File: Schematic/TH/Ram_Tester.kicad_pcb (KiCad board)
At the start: 2 copper layers, 63.3 x 57.2 mm, 42 parts, among them J1 Conn_01x02_Pin, J2 ICSP, Q1 2N7000, Q2 2N7000, SW1 SW_DIP_x03, SW2 SW_Push, U1 ATmega328-P, U2 RAM / ZIF, U3 ZIP Socket, Y1 Crystal

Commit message: v1.1 - minor fix
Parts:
- C5: footprint Capacitor_THT:C_Disc_D4.3mm_W1.9mm_P5.00mm -> Capacitor_THT:CP_Radial_D4.0mm_P2.00mm
- moved C5 2.00 mm to (117.6, 77.0)
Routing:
- net /5V: track 124.3 -> 130.3 mm
- net /GND: track 198.9 -> 199.9 mm, vias 40 -> 38
- net Net-(U1-PC3): track 18.2 -> 18.8 mm

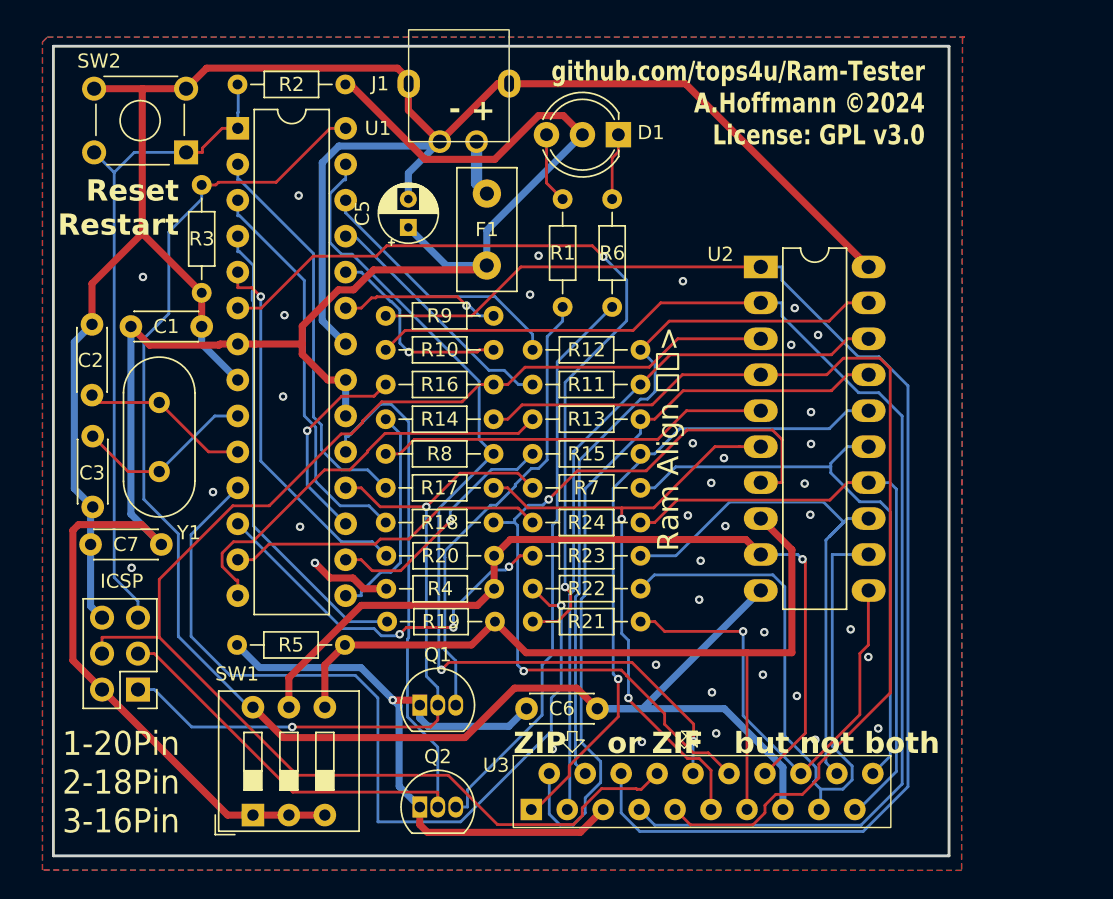
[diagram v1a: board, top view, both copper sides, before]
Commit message: v2 TH Version with Display
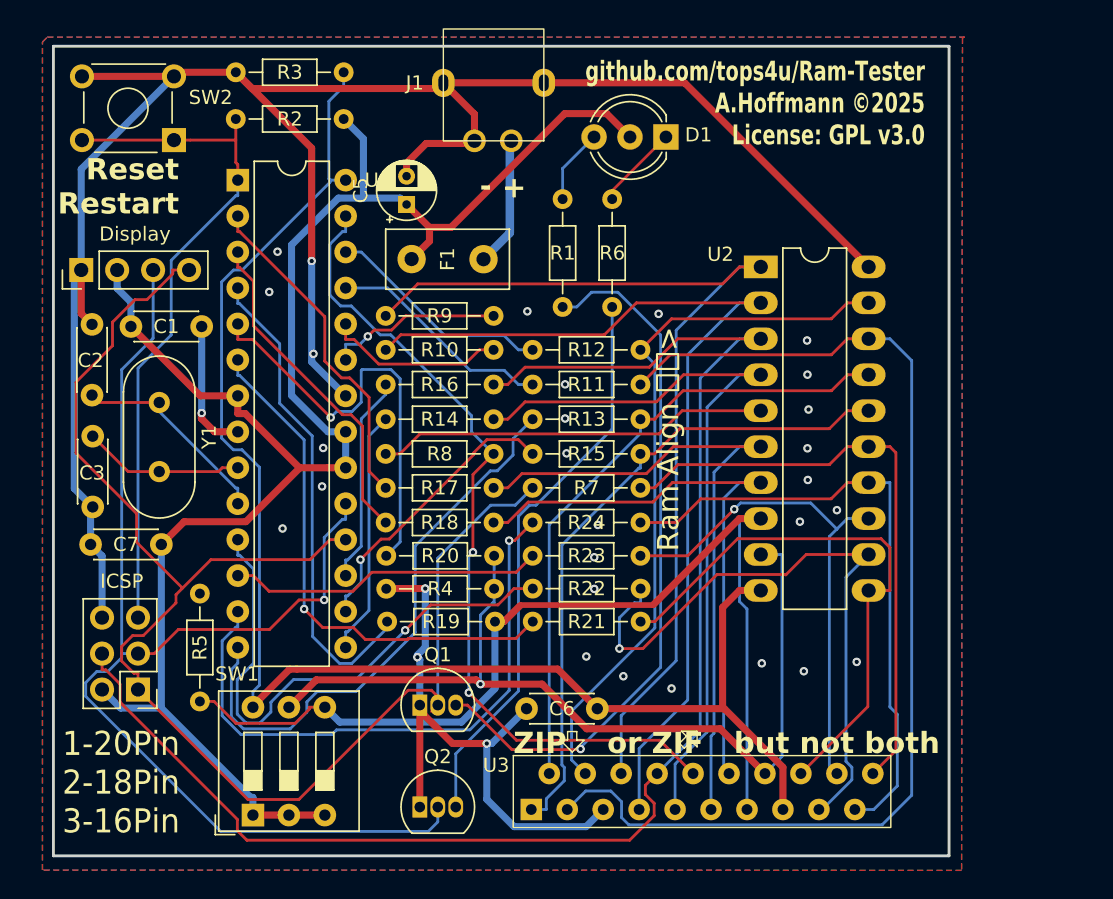
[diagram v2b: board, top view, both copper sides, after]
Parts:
- added Display: Conn_01x04_Pin, Connector_PinHeader_2.54mm:PinHeader_1x04_P2.54mm_Vertical, F.Cu at (94.5, 80.0)
- Y1: footprint Crystal:Crystal_HC49-U_Vertical -> Crystal:Crystal_HC49-4H_Vertical
- moved R3 15.8 mm to (105.4, 66.0), turned to 0 degrees
- moved F1 4.64 mm to (122.9, 79.2), turned to 180 degrees
- moved R5 4.48 mm to (102.9, 102.9), turned to -90 degrees
- moved U1 3.66 mm to (105.5, 73.7)
- moved D1 3.36 mm to (135.8, 70.6)
- moved J1 2.45 mm to (123.6, 76.9)
- moved R2 2.44 mm to (113.0, 69.3)
- moved C5 1.62 mm to (117.5, 75.4)
- moved SW2 1.22 mm to (101.0, 70.8)
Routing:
- net Net-(Display1-Pin_4): track 53.1 -> 101.2 mm, vias 2 -> 0
- net Net-(U2-I/O3): track 49.6 -> 79.2 mm
- net Net-(U2-I/O1): track 95.6 -> 68.7 mm
- net Net-(Display1-Pin_3): track 61.4 -> 86.1 mm, vias 0 -> 1
- net Net-(U1-PD5): track 62.2 -> 38.8 mm
- net Net-(U1-PD4): track 58.5 -> 37.2 mm, vias 2 -> 1
- net Net-(U1-PD7): track 22.8 -> 42.8 mm, vias 0 -> 1
- net Net-(U2-I/O2): track 88.0 -> 68.1 mm
- net Net-(U2-RAS): track 73.4 -> 54.3 mm
- net Net-(Q1-D): track 32.4 -> 50.3 mm, vias 0 -> 1
- net Net-(U2-A1): track 56.8 -> 42.7 mm, vias 2 -> 0
- net Net-(U2-A2): track 59.6 -> 72.3 mm
- net Net-(U1-PB0): track 29.5 -> 40.5 mm
- net Net-(U2-CAS): track 54.1 -> 45.1 mm
- net Net-(U1-PC4): track 66.5 -> 58.9 mm
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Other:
- board text added: "github.com/tops4u/Ram-Tester A.Hoffmann ©2025 License: GPL v3.0"
- board text removed: "github.com/tops4u/Ram-Tester A.Hoffmann ©2024 License: GPL v3.0"
